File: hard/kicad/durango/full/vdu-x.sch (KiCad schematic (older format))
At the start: 47 parts, among them J105 SCART, J4 LED, Q306 BC548, Q4 BC548, Q5 BC548, U124 74HC574, U125 74HC157, U126 HC86, U127 74HC245, U15 74HCT4040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

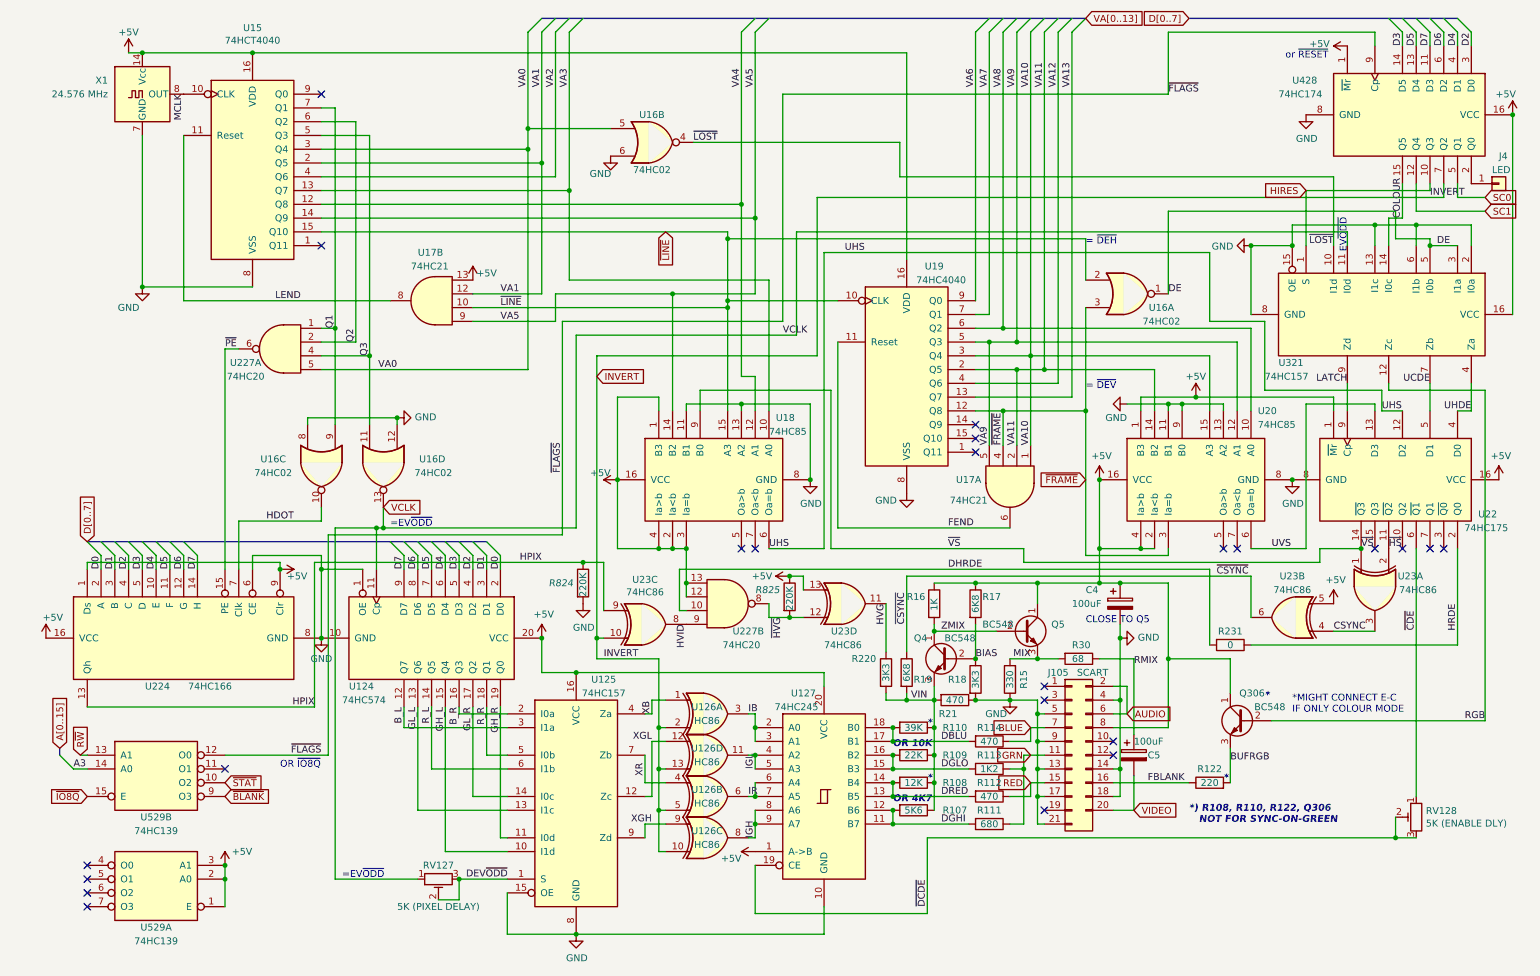
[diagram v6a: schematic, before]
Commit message: add HR DELAY control
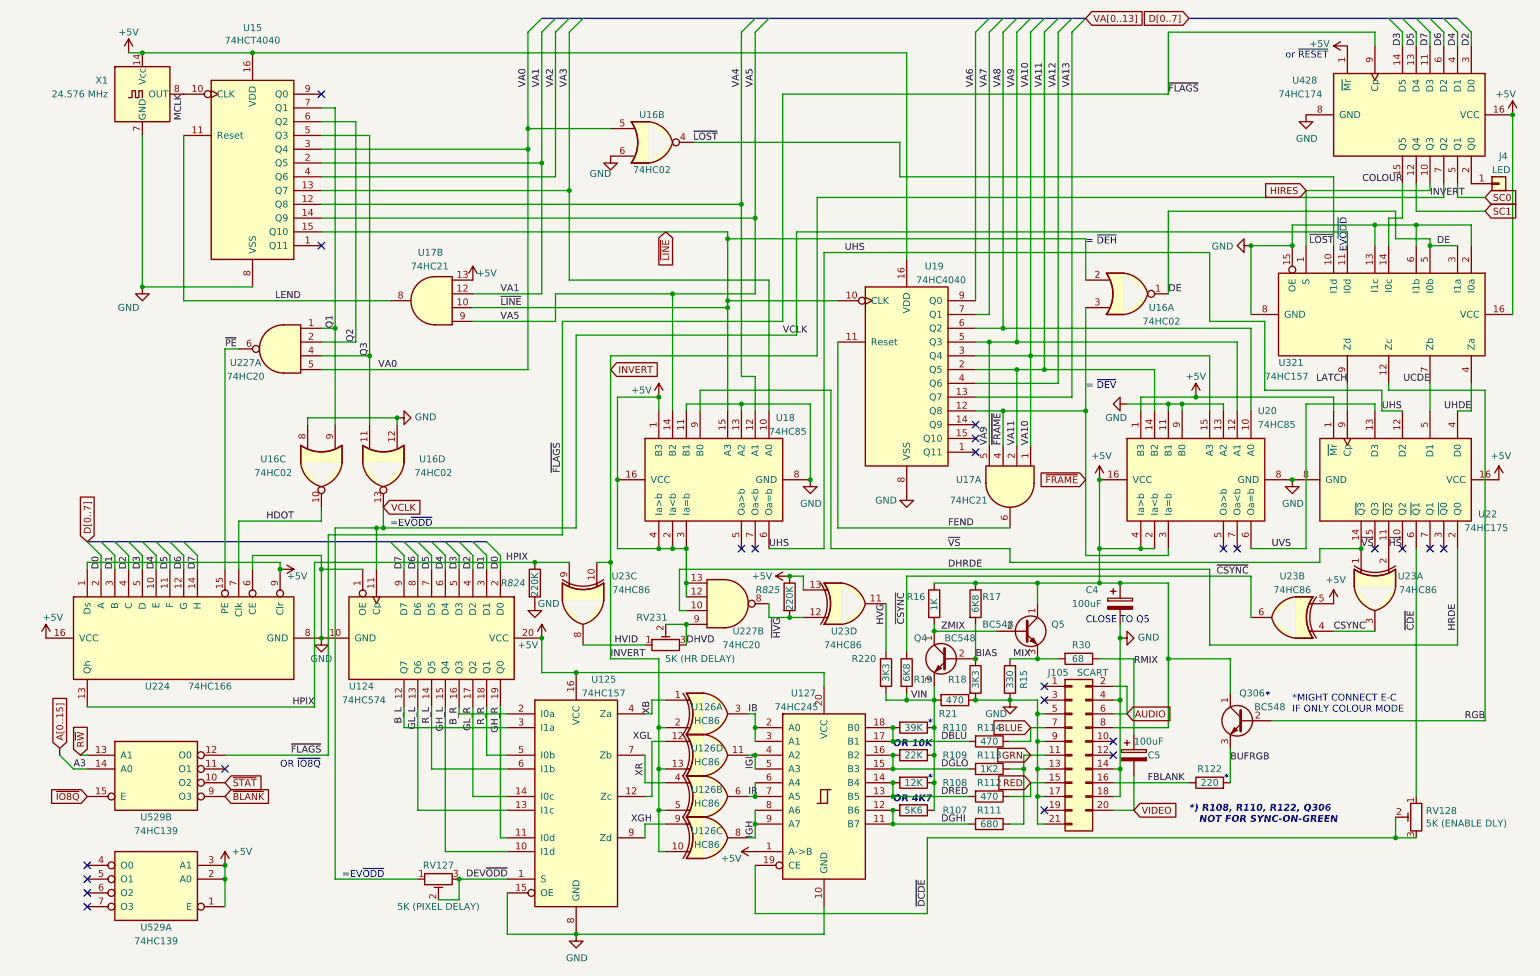
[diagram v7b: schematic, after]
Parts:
- removed R231: 0, Resistor_THT:R_Axial_DIN0207_L6.3mm_D2.5mm_P2.54mm_Vertical, symbol Device:R
- added RV231: 5K (HR DELAY), Potentiometer_THT:Potentiometer_Piher_PT-10-V10_Vertical, symbol Device:R_POT_TRIM
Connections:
- net HRDE is gone; now on net DHRDE: U22.2 (Q0)
- net HVID: now also RV231.1; no longer U227.9
- new net DHVD: RV231.2, RV231.3, U227.9
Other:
- moved on the sheet: R824, U23C
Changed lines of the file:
@@
 L power:+5V #PWR0120
 U 1 1 6080689B
-P 4650 3900
-F 0 "#PWR0120" H 4650 3750 50  0001 C CNN
-F 1 "+5V" V 4700 3950 50  0000 L CNN
-F 2 "" H 4650 3900 50  0001 C CNN
-F 3 "" H 4650 3900 50  0001 C CNN
-	1    4650 3900
-	0    -1   -1   0
+P 4950 3300
+F 0 "#PWR0120" H 4950 3150 50  0001 C CNN
+F 1 "+5V" H 4750 3350 50  0000 L CNN
+F 2 "" H 4950 3300 50  0001 C CNN
+F 3 "" H 4950 3300 50  0001 C CNN
+	1    4950 3300
+	1    0    0    -1
 $EndComp
 $Comp
@@
 P 4100 5050
 F 0 "#PWR0144" H 4100 4900 50  0001 C CNN
-F 1 "+5V" H 4115 5223 50  0000 C CNN
+F 1 "+5V" H 4000 5000 50  0000 C CNN
 F 2 "" H 4100 5050 50  0001 C CNN
 F 3 "" H 4100 5050 50  0001 C CNN
@@
 L 74xx:74HC86 U23
 U 3 1 60DAA11E
-P 4850 4950
-F 0 "U23" H 4850 5275 50  0000 C CNN
-F 1 "74HC86" H 4850 5184 50  0000 C CNN
-F 2 "Package_DIP:DIP-14_W7.62mm_Socket" H 4850 4950 50  0001 C CNN
-F 3 "http://www.ti.com/lit/gpn/sn74HC86" H 4850 4950 50  0001 C CNN
-	3    4850 4950
-	1    0    0    -1
+P 4400 4800
+F 0 "U23" V 4200 4500 50  0000 C CNN
+F 1 "74HC86" V 4300 4450 50  0000 C CNN
+F 2 "Package_DIP:DIP-14_W7.62mm_Socket" H 4400 4800 50  0001 C CNN
+F 3 "http://www.ti.com/lit/gpn/sn74HC86" H 4400 4800 50  0001 C CNN
+	3    4400 4800
+	0    -1   1    0
 $EndComp
 Wire Wire Line
@@
 Text Label 2450 5550 2    50   ~ 0
 HPIX
-Text Label 5150 4950 3    50   ~ 0
+Text Label 4800 5100 2    50   ~ 0
 HVID
 $Comp
 L Device:R R824
 U 1 1 6090A54B
-P 4400 4650
-F 0 "R824" H 4150 4650 50  0000 L CIN
-F 1 "220K" V 4400 4550 50  0000 L CNN
-F 2 "Resistor_THT:R_Axial_DIN0207_L6.3mm_D2.5mm_P2.54mm_Vertical" V 4330 4650 50  0001 C CNN
-F 3 "~" H 4400 4650 50  0001 C CNN
-	1    4400 4650
+P 4050 4650
+F 0 "R824" H 3800 4650 50  0000 L CIN
+F 1 "220K" V 4050 4550 50  0000 L CNN
+F 2 "Resistor_THT:R_Axial_DIN0207_L6.3mm_D2.5mm_P2.54mm_Vertical" V 3980 4650 50  0001 C CNN
+F 3 "~" H 4050 4650 50  0001 C CNN
+	1    4050 4650
 	1    0    0    -1
 $EndComp
@@
 D7
 Wire Wire Line
-	4500 3000 6100 3000
+	4600 3000 6100 3000
 $Comp
 L Transistor_BJT:BC547 Q306
@@
 	9100 5200 9100 5450
 Wire Wire Line
-	4550 4500 4400 4500
+	4300 4500 4050 4500
 Wire Wire Line
 	2450 4500 2450 5550
@@
 	4950 5700 4950 5200
 Wire Wire Line
-	4950 5200 4500 5200
+	4950 5200 4600 5200
 Connection ~ 4950 5700
-Wire Wire Line
-	4550 4500 4550 4850
-Text Label 4550 5200 0    50   ~ 0
+Text Label 4600 5200 0    50   ~ 0
 INVERT
-Connection ~ 4400 4500
-Wire Wire Line
-	4400 4500 2450 4500
+Connection ~ 4050 4500
+Wire Wire Line
+	4050 4500 2450 4500
 $Comp
 L power:GND #PWR0142
 U 1 1 6278CB06
-P 4400 4800
-F 0 "#PWR0142" H 4400 4550 50  0001 C CNN
-F 1 "GND" H 4405 4627 50  0000 C CNN
-F 2 "" H 4400 4800 50  0001 C CNN
-F 3 "" H 4400 4800 50  0001 C CNN
-	1    4400 4800
+P 4050 4800
+F 0 "#PWR0142" H 4050 4550 50  0001 C CNN
+F 1 "GND" H 4150 4800 50  0000 C CNN
+F 2 "" H 4050 4800 50  0001 C CNN
+F 3 "" H 4050 4800 50  0001 C CNN
+	1    4050 4800
 	1    0    0    -1
 $EndComp
@@
 	0    -1   1    0
 $EndComp
-Wire Wire Line
-	4500 5050 4500 5200
-Connection ~ 4500 5050
 NoConn ~ 10650 4400
 Connection ~ 5150 4400
-Wire Wire Line
-	4500 3000 4500 5050
-Wire Wire Line
-	4500 5050 4550 5050
 $Comp
 L power:+5V #PWR0163
@@
 Wire Wire Line
 	6000 4600 6000 4700
-Text GLabel 4500 3150 2    50   Input ~ 0
+Text GLabel 4600 3100 2    50   Input ~ 0
 INVERT
 Text GLabel 8050 3900 0    50   Input ~ 0
@@
 Text Label 6750 4950 1    50   ~ 0
 ~CSYNC
-Text Label 4100 4500 2    50   ~ 0
+Text Label 4000 4500 2    50   ~ 0
 HPIX
 Wire Wire Line
@@
 Wire Wire Line
 	10250 2000 10350 2000
-Text Label 10350 2000 1    50   ~ 0
+Text Label 10350 1750 2    50   ~ 0
 COLOUR
-$Comp
-L Device:R R231
-U 1 1 621963F6
-P 9100 5100
-F 0 "R231" V 9000 5100 50  0000 C CNN
-F 1 "0" V 9100 5100 50  0000 C CNN
-F 2 "Resistor_THT:R_Axial_DIN0207_L6.3mm_D2.5mm_P2.54mm_Vertical" V 9030 5100 50  0001 C CNN
-F 3 "~" H 9100 5100 50  0001 C CNN
-	1    9100 5100
-	0    1    1    0
-$EndComp
-Wire Wire Line
-	9250 5100 10750 5100
+Wire Wire Line
+	8950 5100 10750 5100
 Connection ~ 3050 3450
 Connection ~ 8300 4650
@@
 	9750 4400 9750 4500
 Wire Wire Line
-	9750 4500 7600 4500
-Wire Wire Line
-	7600 4500 7600 4400
-Wire Wire Line
-	7600 4400 6200 4400
+	9750 4500 7500 4500
+Wire Wire Line
+	7500 4500 7500 4400
+Wire Wire Line
+	7500 4400 6200 4400
 Connection ~ 10050 4400
 Text Label 7050 4400 0    50   ~ 0
@@
 Wire Wire Line
 	10300 6500 10450 6500
-Wire Bus Line
-	8800 550  10750 550
-Wire Bus Line
-	4100 550  8050 550
-Wire Bus Line
-	800  4350 3700 4350
 Text Notes 3000 4250 0    50   ~ 0
 =EV~ODD
@@
 Wire Wire Line
 	8400 6300 8250 6300
+Connection ~ 4950 3300
+Wire Wire Line
+	4500 4500 4600 4500
+Wire Wire Line
+	4600 3000 4600 4500
+Connection ~ 4600 4500
+Wire Wire Line
+	4600 4500 4600 5200
+$Comp
+L Device:R_POT_TRIM RV231
+U 1 1 62BC55A0
+P 5000 5100
+F 0 "RV231" V 5200 5200 50  0000 C CNN
+F 1 "5K (HR DELAY)" V 4900 4850 50  0000 C CNN
+F 2 "Potentiometer_THT:Potentiometer_Piher_PT-10-V10_Vertical" H 5000 5100 50  0001 C CNN
+F 3 "~" H 5000 5100 50  0001 C CNN
+	1    5000 5100
+	0    -1   -1   0
+$EndComp
+Wire Wire Line
+	4850 5100 4400 5100
+Text Label 5150 5100 0    50   ~ 0
+DHVD
+Wire Wire Line
+	5150 5100 5150 4950
+Wire Wire Line
+	5000 4950 5150 4950
+Connection ~ 5150 4950
+Wire Bus Line
+	8800 550  10750 550
+Wire Bus Line
+	4100 550  8050 550
+Wire Bus Line
+	800  4350 3700 4350
 $EndSCHEMATC

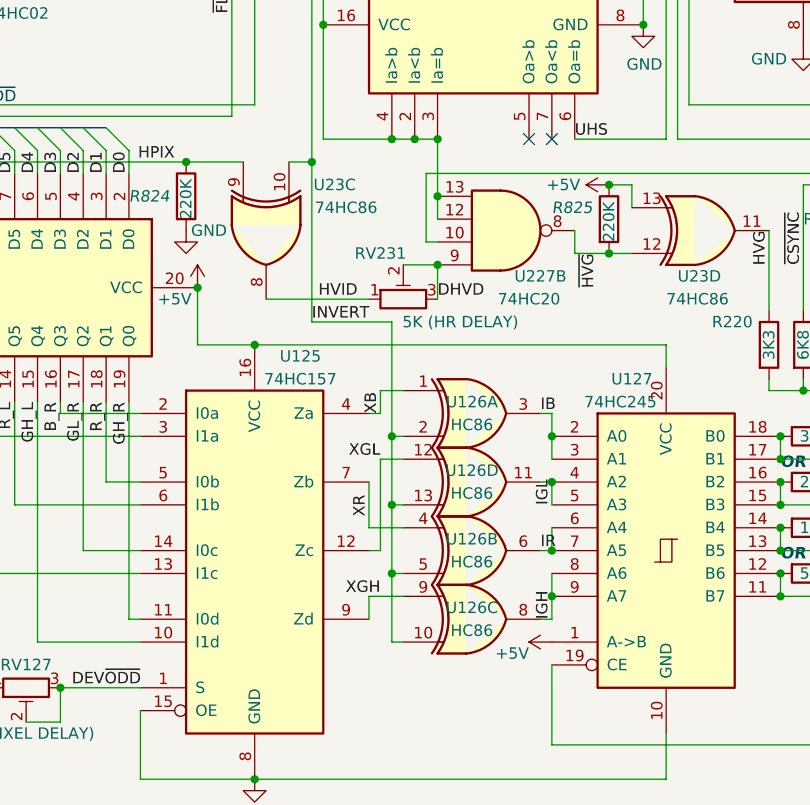
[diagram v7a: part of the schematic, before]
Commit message: remove EPROM and change LEDs
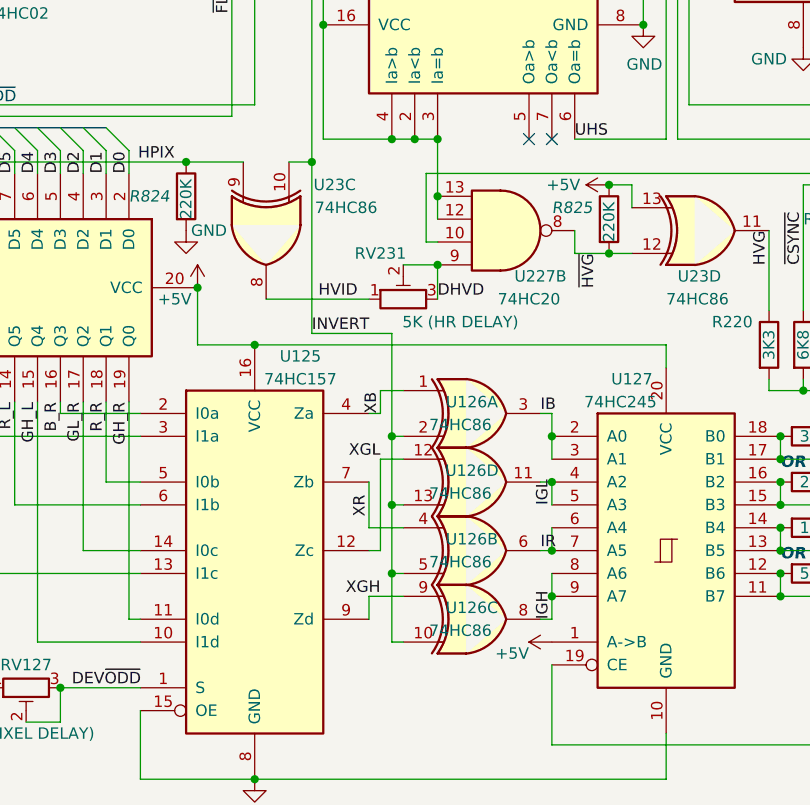
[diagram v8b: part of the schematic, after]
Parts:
- U126: value HC86 -> 74HC86
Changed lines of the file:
@@
 P 5300 5600
 F 0 "U126" H 5300 5650 50  0000 C CNN
-F 1 "HC86" H 5300 5550 50  0000 C CNN
+F 1 "74HC86" H 5250 5550 50  0000 C CNN
 F 2 "Package_DIP:DIP-14_W7.62mm_Socket" H 5300 5600 50  0001 C CNN
 F 3 "http://www.ti.com/lit/gpn/sn74HC86" H 5300 5600 50  0001 C CNN
@@
 P 5300 6200
 F 0 "U126" H 5300 6250 50  0000 C CNN
-F 1 "HC86" H 5300 6150 50  0000 C CNN
+F 1 "74HC86" H 5250 6150 50  0000 C CNN
 F 2 "Package_DIP:DIP-14_W7.62mm_Socket" H 5300 6200 50  0001 C CNN
 F 3 "http://www.ti.com/lit/gpn/sn74HC86" H 5300 6200 50  0001 C CNN
@@
 P 5300 6500
 F 0 "U126" H 5300 6550 50  0000 C CNN
-F 1 "HC86" H 5300 6450 50  0000 C CNN
+F 1 "74HC86" H 5250 6450 50  0000 C CNN
 F 2 "Package_DIP:DIP-14_W7.62mm_Socket" H 5300 6500 50  0001 C CNN
 F 3 "http://www.ti.com/lit/gpn/sn74HC86" H 5300 6500 50  0001 C CNN
@@
 P 5300 5900
 F 0 "U126" H 5300 5950 50  0000 C CNN
-F 1 "HC86" H 5300 5850 50  0000 C CNN
+F 1 "74HC86" H 5250 5850 50  0000 C CNN
 F 2 "Package_DIP:DIP-14_W7.62mm_Socket" H 5300 5900 50  0001 C CNN
 F 3 "http://www.ti.com/lit/gpn/sn74HC86" H 5300 5900 50  0001 C CNN
@@
 Connection ~ 4100 5050
 Wire Wire Line
-	4950 5700 4950 5200
-Wire Wire Line
-	4950 5200 4600 5200
+	4950 5700 4950 5250
+Wire Wire Line
+	4950 5250 4600 5250
 Connection ~ 4950 5700
-Text Label 4600 5200 0    50   ~ 0
+Text Label 4600 5250 0    50   ~ 0
 INVERT
 Connection ~ 4050 4500
@@
 Connection ~ 4600 4500
 Wire Wire Line
-	4600 4500 4600 5200
+	4600 4500 4600 5250
 $Comp
 L Device:R_POT_TRIM RV231
